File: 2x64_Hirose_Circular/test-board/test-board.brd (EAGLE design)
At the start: 152.4 x 168.9 mm, 76 parts

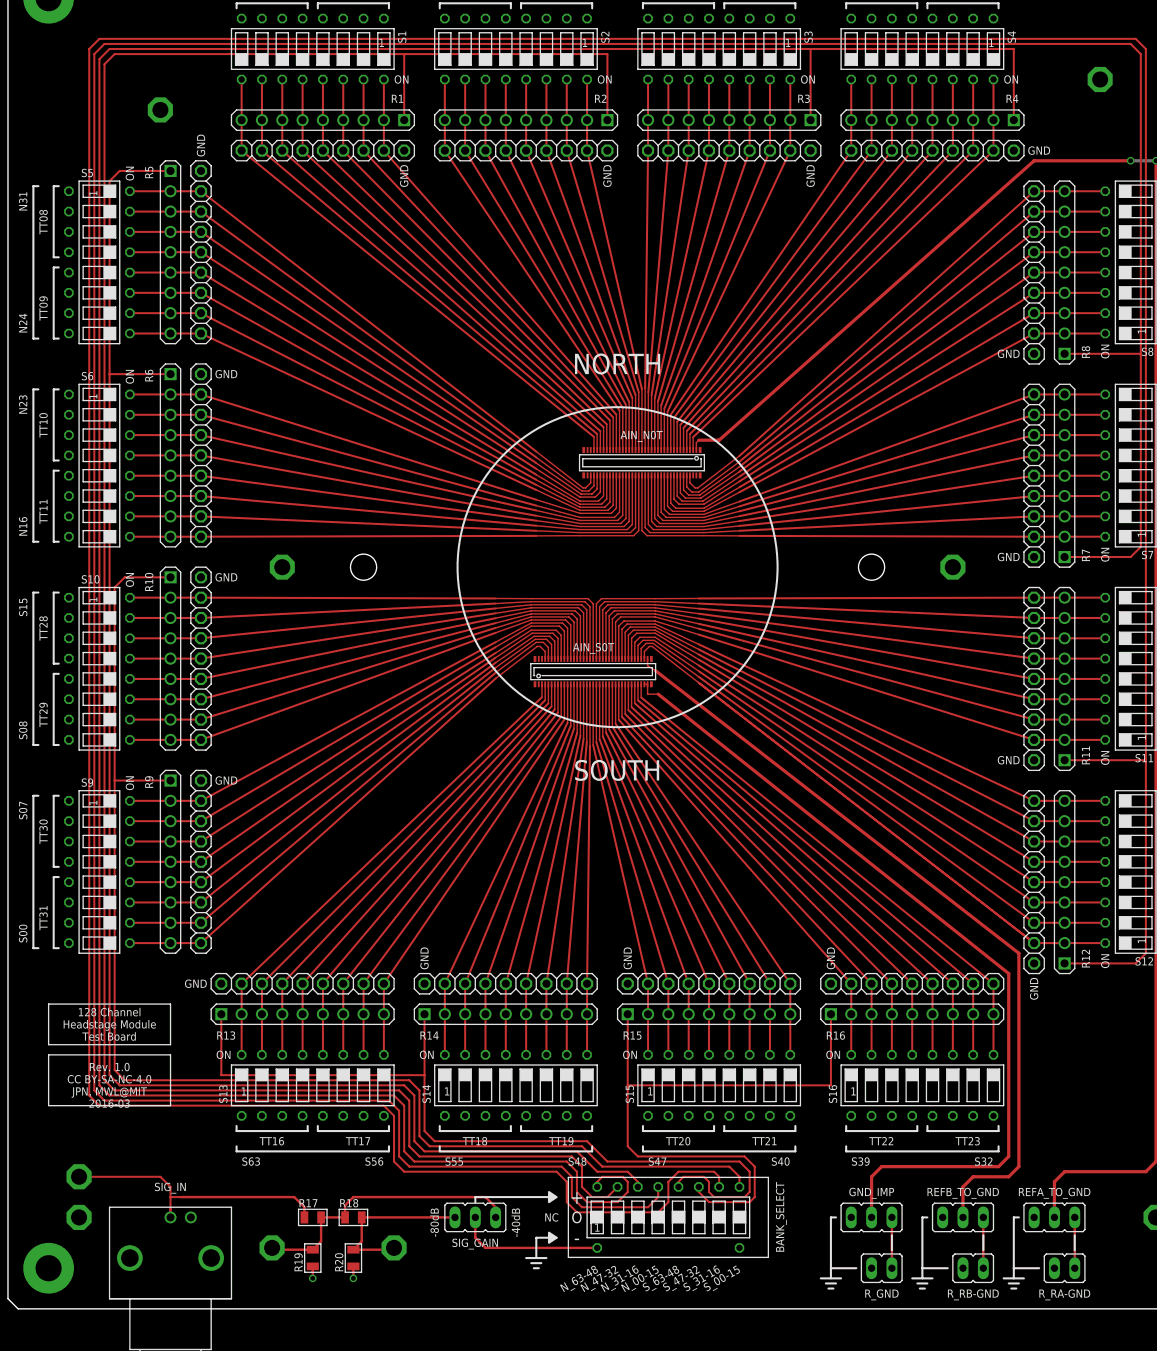
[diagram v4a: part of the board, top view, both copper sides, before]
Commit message: Revsion 1.0 of 128 channel test board sent to fab.
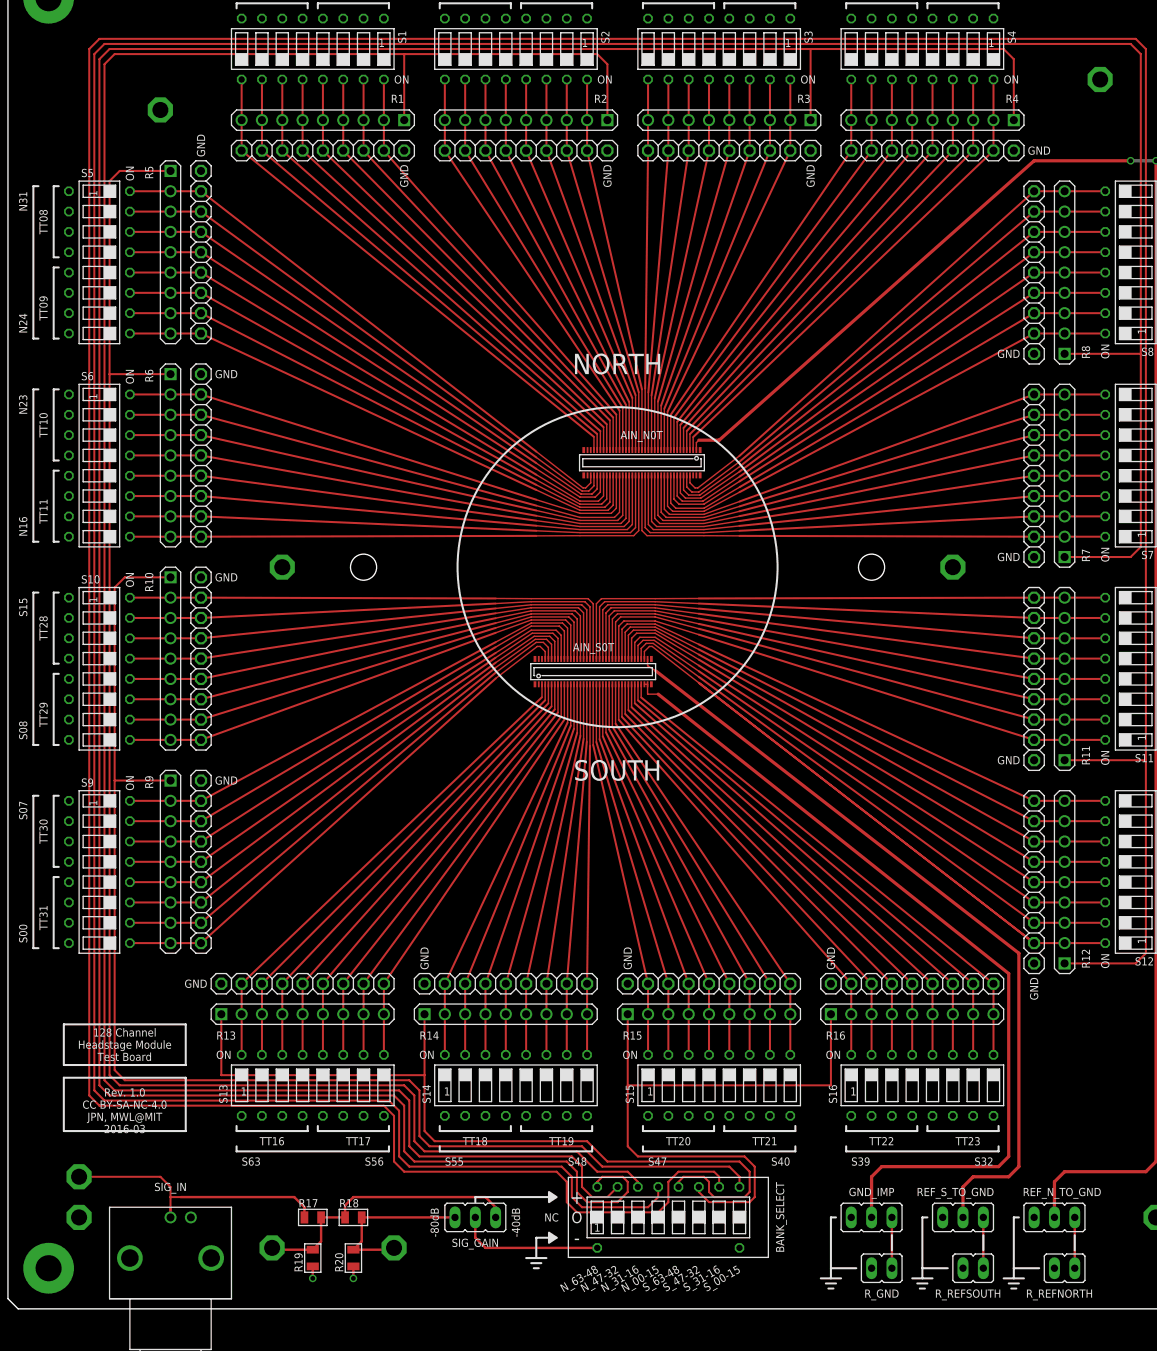
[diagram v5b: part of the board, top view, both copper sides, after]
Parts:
- S1, S10, S11, S12, S13, S14, S15, S16, S2, S3, S4, S5, S6, S7, S8, S9: value (none) -> ADE
- renumbered REFA_TO_GND to REF_N_TO_GND, REFB_TO_GND to REF_S_TO_GND, R_RA-GND to R_REFNORTH, R_RB-GND to R_REFSOUTH
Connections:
- net REF_A renamed REF_NORTH
- net REF_B renamed REF_SOUTH
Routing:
- net SIG_N_63-48: track 344.6 -> 343.8 mm
- net SIG_N_47-32: track 282.4 -> 281.7 mm
